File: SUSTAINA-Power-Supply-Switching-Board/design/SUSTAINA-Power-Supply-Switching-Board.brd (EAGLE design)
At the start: 75 x 50 mm, 67 parts, among them IC1 LTC4418IUF, M1 POWER-MONITOR-MODULE, M2 POWER-MONITOR-MODULE, U1 SI7997DP-T1-GE3, U2 SI7997DP-T1-GE3

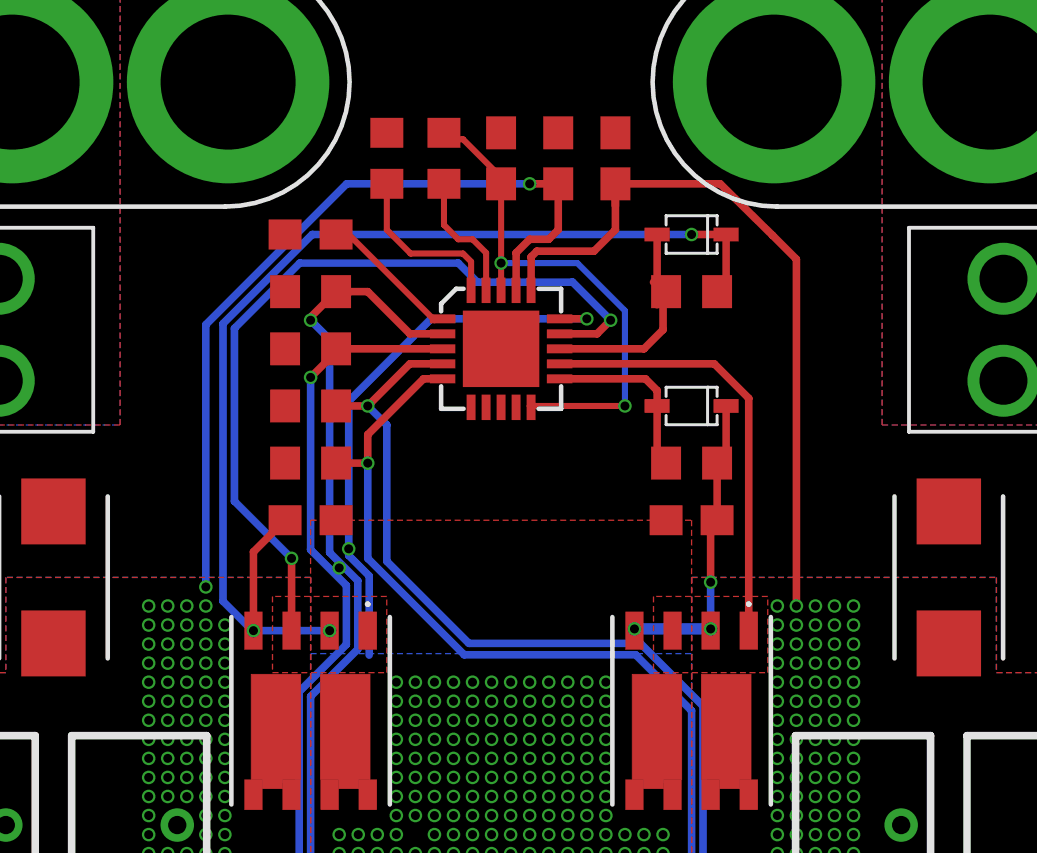
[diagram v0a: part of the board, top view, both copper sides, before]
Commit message: Corrected a via error and added some capacitors
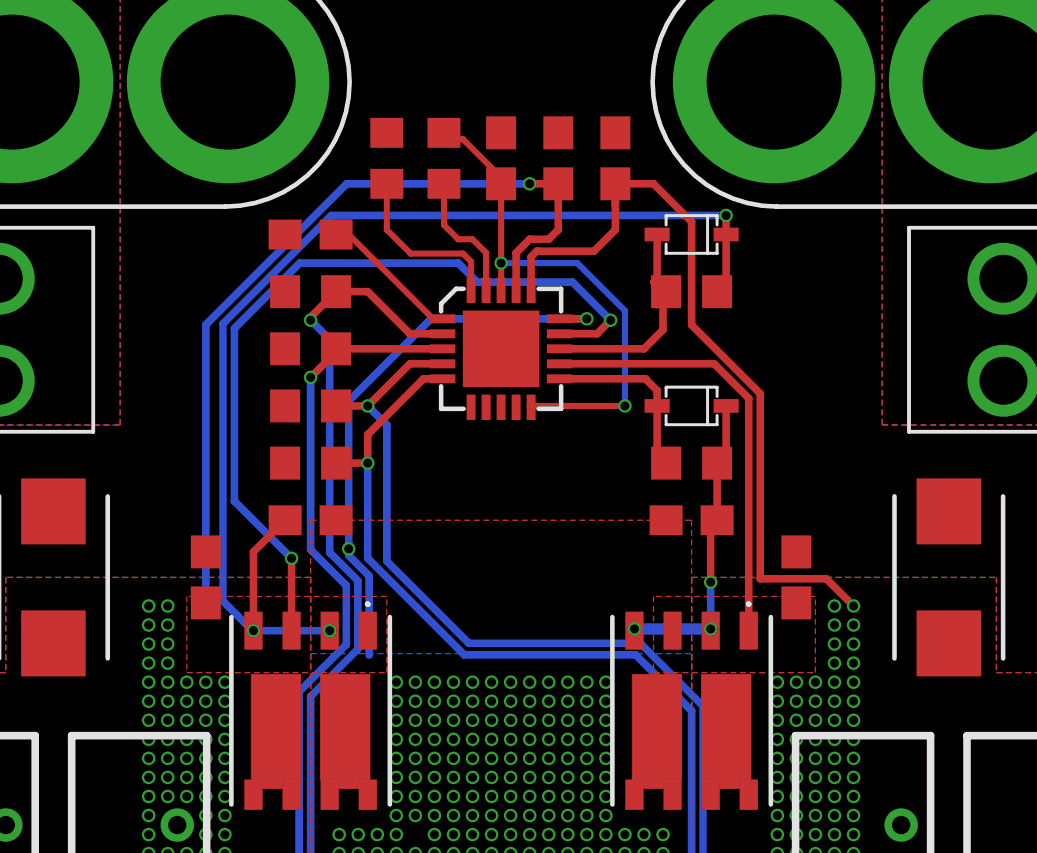
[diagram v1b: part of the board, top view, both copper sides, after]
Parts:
- added C10, C9: 1u, rcl:C0603
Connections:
- net GND: now also C10.2, C9.2
- net VS1: now also C9.1
- net VS2: now also C10.1
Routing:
- net G1: track 38.0 -> 38.9 mm
- net PWR_IN2_: track 29.5 -> 30.3 mm, vias 90 -> 78
- net PWR_OUT: vias 134 -> 133
- net PWR_IN1_: vias 87 -> 75
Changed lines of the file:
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@@
 <drawing>
 <settings>
-<setting alwaysvectorfont="no"/>
+<setting alwaysvectorfont="yes"/>
 <setting verticaltext="up"/>
 </settings>
@@
 <element name="U$3" library="buzzard_labels" package="1ST_PRIORITY" value="" x="-21.59" y="48.5775" smashed="yes" rot="R270"/>
 <element name="U$4" library="buzzard_labels" package="2ND_PRIORITY" value="" x="21.59" y="41.275" smashed="yes" rot="R90"/>
+<element name="C9" library="rcl" library_urn="urn:adsk.eagle:library:334" package="C0603" package3d_urn="urn:adsk.eagle:package:23616/2" value="1u" x="-9.8425" y="28.575" smashed="yes" rot="R90">
+<attribute name="POPULARITY" value="37" x="-9.8425" y="28.575" size="1.778" layer="27" rot="R90" display="off"/>
+<attribute name="SPICEPREFIX" value="C" x="-9.8425" y="28.575" size="1.778" layer="27" rot="R90" display="off"/>
+<attribute name="VALUE" x="-7.9375" y="27.94" size="1.27" layer="27" rot="R90"/>
+</element>
+<element name="C10" library="rcl" library_urn="urn:adsk.eagle:library:334" package="C0603" package3d_urn="urn:adsk.eagle:package:23616/2" value="1u" x="9.8425" y="28.575" smashed="yes" rot="R90">
+<attribute name="POPULARITY" value="37" x="9.8425" y="28.575" size="1.778" layer="27" rot="R90" display="off"/>
+<attribute name="SPICEPREFIX" value="C" x="9.8425" y="28.575" size="1.778" layer="27" rot="R90" display="off"/>
+<attribute name="VALUE" x="11.7475" y="27.94" size="1.27" layer="27" rot="R90"/>
+</element>
 </elements>
 <signals>
@@
 <contactref element="CH4" pad="-"/>
 <contactref element="CH5" pad="1"/>
+<contactref element="C9" pad="2"/>
+<contactref element="C10" pad="2"/>
 </signal>
 <signal name="PWR_IN1_FUSE" class="2">
@@
 <vertex x="5.08" y="27.94"/>
 <vertex x="5.08" y="25.4"/>
-<vertex x="8.89" y="25.4"/>
-<vertex x="8.89" y="27.94"/>
+<vertex x="10.4775" y="25.4"/>
+<vertex x="10.4775" y="27.94"/>
 </polygon>
 <wire x1="1.95" y1="35.695" x2="7.1042125" y2="35.695" width="0.254" layer="1"/>
 <wire x1="7.1042125" y1="35.695" x2="8.255" y2="34.5442125" width="0.254" layer="1"/>
 <wire x1="8.255" y1="34.5442125" x2="8.255" y2="26.8" width="0.254" layer="1"/>
+<contactref element="C10" pad="1"/>
 </signal>
 <signal name="G2" class="6">
@@
 <wire x1="7.2" y1="38.1" x2="7.5175" y2="37.7825" width="0.254" layer="1"/>
 <wire x1="7.5175" y1="37.7825" x2="7.5" y2="37.7825" width="0.254" layer="1"/>
-<via x="6.35" y="40.005" extent="1-16" drill="0.3"/>
-<wire x1="6.35" y1="40.005" x2="7.5" y2="40.005" width="0.254" layer="1"/>
-<wire x1="-6.297925" y1="40.005" x2="6.35" y2="40.005" width="0.254" layer="16"/>
+<via x="7.5" y="40.64" extent="1-16" drill="0.3"/>
+<wire x1="7.5" y1="40.64" x2="7.5" y2="40.005" width="0.254" layer="1"/>
+<wire x1="-5.662925" y1="40.64" x2="7.5" y2="40.64" width="0.254" layer="16"/>
 <contactref element="U1" pad="2"/>
 <contactref element="U1" pad="4"/>
@@
 <via x="-5.715" y="26.8" extent="1-16" drill="0.3"/>
 <wire x1="-8.255" y1="26.8" x2="-5.715" y2="26.8" width="0.254" layer="16"/>
-<wire x1="-9.271" y1="37.031925" x2="-6.297925" y2="40.005" width="0.254" layer="16"/>
+<wire x1="-9.271" y1="37.031925" x2="-5.662925" y2="40.64" width="0.254" layer="16"/>
 <wire x1="-8.255" y1="26.8" x2="-8.379" y2="26.924" width="0.254" layer="16"/>
 <wire x1="-8.379" y1="26.924" x2="-8.41281875" y2="26.924" width="0.254" layer="16"/>
@@
 <contactref element="IC1" pad="14"/>
 <polygon width="0.254" layer="1" thermals="no">
-<vertex x="-7.62" y="27.94"/>
-<vertex x="-7.62" y="25.4"/>
+<vertex x="-10.4775" y="27.94"/>
+<vertex x="-10.4775" y="25.4"/>
 <vertex x="-3.81" y="25.4"/>
 <vertex x="-3.81" y="27.94"/>
@@
 <wire x1="-6.985" y1="29.21" x2="-8.89" y2="31.115" width="0.254" layer="16"/>
 <wire x1="-6.985" y1="29.21" x2="-6.985" y2="27.305" width="0.254" layer="1"/>
+<contactref element="C9" pad="1"/>
 </signal>
 <signal name="PWR_OUT" class="2">
@@
 <via x="-2.8575" y="21.2725" extent="1-16" drill="0.3"/>
 <via x="-2.8575" y="20.6375" extent="1-16" drill="0.3"/>
-<via x="-5.3975" y="28.8925" extent="1-16" drill="0.3"/>
 <via x="-2.8575" y="19.3675" extent="1-16" drill="0.3"/>
 <via x="0.9525" y="21.9075" extent="1-16" drill="0.3"/>
@@
 <wire x1="1.905" y1="40.16375" x2="1.905" y2="41.695" width="0.254" layer="1"/>
 <wire x1="0.5" y1="39.39375" x2="0.9525" y2="39.84625" width="0.254" layer="1"/>
-<via x="-9.8425" y="28.2575" extent="1-16" drill="0.3"/>
 <contactref element="R12" pad="2"/>
 <contactref element="R17" pad="2"/>
@@
 <via x="-11.1125" y="25.7175" extent="1-16" drill="0.3"/>
 <via x="-11.1125" y="26.3525" extent="1-16" drill="0.3"/>
-<via x="-10.4775" y="25.7175" extent="1-16" drill="0.3"/>
 <via x="-9.8425" y="25.0825" extent="1-16" drill="0.3"/>
 <via x="-9.2075" y="24.4475" extent="1-16" drill="0.3"/>
 <via x="-9.2075" y="25.0825" extent="1-16" drill="0.3"/>
-<via x="-9.8425" y="25.7175" extent="1-16" drill="0.3"/>
-<via x="-10.4775" y="26.3525" extent="1-16" drill="0.3"/>
-<via x="-9.8425" y="26.3525" extent="1-16" drill="0.3"/>
-<via x="-9.2075" y="25.7175" extent="1-16" drill="0.3"/>
-<via x="-9.2075" y="26.3525" extent="1-16" drill="0.3"/>
 <via x="-11.1125" y="26.9875" extent="1-16" drill="0.3"/>
-<via x="-10.4775" y="26.9875" extent="1-16" drill="0.3"/>
-<via x="-9.2075" y="26.9875" extent="1-16" drill="0.3"/>
-<via x="-9.8425" y="26.9875" extent="1-16" drill="0.3"/>
-<via x="-9.8425" y="27.6225" extent="1-16" drill="0.3"/>
-<via x="-10.4775" y="27.6225" extent="1-16" drill="0.3"/>
 <via x="-11.1125" y="27.6225" extent="1-16" drill="0.3"/>
 <via x="-11.7475" y="27.6225" extent="1-16" drill="0.3"/>
@@
 </polygon>
 <wire x1="3.81" y1="41.695" x2="3.81" y2="40.9575" width="0.254" layer="1"/>
-<wire x1="7.3025" y1="41.695" x2="3.81" y2="41.695" width="0.254" layer="1"/>
-<wire x1="7.3025" y1="41.695" x2="9.04875" y2="39.975653125" width="0.254" layer="1"/>
+<wire x1="3.81" y1="41.695" x2="5.08" y2="41.695" width="0.254" layer="1"/>
 <wire x1="1" y1="38.145" x2="1" y2="39.25875" width="0.254" layer="1"/>
 <wire x1="1.190625" y1="39.449375" x2="3.095625" y2="39.449375" width="0.254" layer="1"/>
@@
 <via x="9.8425" y="20.0025" extent="1-16" drill="0.3"/>
 <via x="9.8425" y="19.3675" extent="1-16" drill="0.3"/>
-<via x="9.2075" y="27.6225" extent="1-16" drill="0.3"/>
-<via x="9.2075" y="26.9875" extent="1-16" drill="0.3"/>
-<via x="9.2075" y="26.3525" extent="1-16" drill="0.3"/>
-<via x="9.2075" y="25.7175" extent="1-16" drill="0.3"/>
 <via x="11.7475" y="27.6225" extent="1-16" drill="0.3"/>
 <via x="11.7475" y="26.9875" extent="1-16" drill="0.3"/>
@@
 <via x="11.1125" y="26.3525" extent="1-16" drill="0.3"/>
 <via x="11.1125" y="25.7175" extent="1-16" drill="0.3"/>
-<via x="10.4775" y="27.6225" extent="1-16" drill="0.3"/>
-<via x="10.4775" y="26.9875" extent="1-16" drill="0.3"/>
-<via x="10.4775" y="26.3525" extent="1-16" drill="0.3"/>
-<via x="10.4775" y="25.7175" extent="1-16" drill="0.3"/>
-<via x="9.8425" y="27.6225" extent="1-16" drill="0.3"/>
-<via x="9.8425" y="26.9875" extent="1-16" drill="0.3"/>
-<via x="9.8425" y="26.3525" extent="1-16" drill="0.3"/>
-<via x="9.8425" y="25.7175" extent="1-16" drill="0.3"/>
 <via x="9.2075" y="18.7325" extent="1-16" drill="0.3"/>
 <via x="9.2075" y="18.0975" extent="1-16" drill="0.3"/>
@@
 <via x="9.8425" y="17.4625" extent="1-16" drill="0.3"/>
 <via x="9.8425" y="16.8275" extent="1-16" drill="0.3"/>
-<wire x1="9.04875" y1="39.975653125" x2="9.8425" y2="39.181903125" width="0.254" layer="1"/>
-<wire x1="9.8425" y1="39.181903125" x2="9.8425" y2="27.6225" width="0.254" layer="1"/>
 <wire x1="8.255" y1="9.105" x2="9.9822" y2="10.8322" width="0.254" layer="1"/>
 <wire x1="9.9822" y1="10.8322" x2="9.9822" y2="12.7" width="0.254" layer="1"/>
+<wire x1="5.08" y1="41.695" x2="6.35" y2="40.425" width="0.254" layer="1"/>
+<wire x1="6.35" y1="40.425" x2="6.35" y2="36.98803125" width="0.254" layer="1"/>
+<wire x1="8.636" y1="34.70203125" x2="8.636" y2="28.529" width="0.254" layer="1"/>
+<wire x1="6.35" y1="36.98803125" x2="8.636" y2="34.70203125" width="0.254" layer="1"/>
+<wire x1="10.841" y1="28.529" x2="8.636" y2="28.529" width="0.254" layer="1"/>
+<wire x1="10.841" y1="28.529" x2="11.7475" y2="27.6225" width="0.254" layer="1"/>
 </signal>
 <signal name="PWR_IN!_FUSE">
